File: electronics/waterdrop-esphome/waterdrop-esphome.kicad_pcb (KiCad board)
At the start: 4 copper layers, 45.7 x 80 mm, 16 parts, among them J1 Barrel_Jack, U1 LM2596DS-ADJ, U2 ESP32-S3-Tiny

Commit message: Schematics are ready for PCB layout
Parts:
- added D3: 1N4148, Diode_SMD:D_SOD-123, F.Cu at (174.0, 105.9)
- added H1: 12V_OUT_RELIEF, MountingHole:MountingHole_4.3mm_M4, F.Cu at (189.1, 71.0)
- added H2: Comm_RO_RELIEF, MountingHole:MountingHole_4.3mm_M4, F.Cu at (189.1, 81.2)
- added J2: 12V_OUT, Connector_Wire:SolderWire-1.5sqmm_1x02_P6mm_D1.7mm_OD3mm_Relief, F.Cu at (175.2, 68.6)
- added J3: Comm_RO, Connector_Wire:SolderWire-0.25sqmm_1x04_P4.2mm_D0.65mm_OD1.7mm_Relief, F.Cu at (187.9, 91.3)
- added J4: Comm_Faucet, Connector_PinHeader_2.54mm:PinHeader_1x05_P2.54mm_Horizontal, F.Cu at (174.7, 91.6)
- added J5: Valve, Connector_PinHeader_2.54mm:PinHeader_1x02_P2.54mm_Horizontal, F.Cu at (156.7, 104.2)
- added K1: G5LE-1, Relay_THT:Relay_SPDT_Omron-G5LE-1, F.Cu at (163.4, 69.4)
- added Q1: BC817, Package_TO_SOT_SMD:SOT-23, F.Cu at (196.6, 85.3)
- added R10: 50k, Resistor_SMD:R_0805_2012Metric_Pad1.20x1.40mm_HandSolder, F.Cu at (161.5, 100.5)
- added R11: 10k, Resistor_SMD:R_0805_2012Metric_Pad1.20x1.40mm_HandSolder, F.Cu at (166.3, 91.6)
- added R12: 50k, Resistor_SMD:R_0805_2012Metric_Pad1.20x1.40mm_HandSolder, F.Cu at (166.3, 94.6)
- added R13: 100k, Resistor_SMD:R_0805_2012Metric_Pad1.20x1.40mm_HandSolder, F.Cu at (166.3, 97.5)
- added R14: 1Ω, Resistor_SMD:R_0805_2012Metric_Pad1.20x1.40mm_HandSolder, F.Cu at (166.3, 100.5)
- added R4: 100k, Resistor_SMD:R_0805_2012Metric_Pad1.20x1.40mm_HandSolder, F.Cu at (156.8, 94.6)
- added R5: 100k, Resistor_SMD:R_0805_2012Metric_Pad1.20x1.40mm_HandSolder, F.Cu at (156.8, 97.5)
- added R6: 100k, Resistor_SMD:R_0805_2012Metric_Pad1.20x1.40mm_HandSolder, F.Cu at (156.8, 100.5)
- added R7: 50k, Resistor_SMD:R_0805_2012Metric_Pad1.20x1.40mm_HandSolder, F.Cu at (161.5, 91.6)
- added R8: 10k, Resistor_SMD:R_0805_2012Metric_Pad1.20x1.40mm_HandSolder, F.Cu at (161.5, 94.6)
- added R9: 100k, Resistor_SMD:R_0805_2012Metric_Pad1.20x1.40mm_HandSolder, F.Cu at (161.5, 97.5)
- added U3: 74AHCT125, Package_SO:SOIC-14_3.9x8.7mm_P1.27mm, F.Cu at (198.4, 71.2)
- added U4: TB67H450A, Package_SO:SOIC-8-1EP_3.9x4.9mm_P1.27mm_EP2.29x3mm_ThermalVias, F.Cu at (198.4, 79.7)
- D1: footprint Diode_SMD:D_SMA -> Diode_SMD:D_SMA_Handsoldering
- J1: value Barrel_Jack -> 12V_IN
- JP1: value 3V3 -> 5V
- R1: value 2k -> 3.6k
- R3: value 100k -> 10k
- moved R3 27.3 mm to (156.8, 91.6)
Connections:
- net /Power supply/SUPPLY_12V renamed /12V_IN
- J1 pad 3: (no net) -> unconnected-(J1-Pad3)
- JP1 pad 2: +3.3V -> +5V
- R3 pad 1: GND -> Net-(Q1-B)
- R3 pad 2: Net-(U2-5V) -> /12V_control
- U2 pad 1: Net-(U2-5V) -> +5V
- U2 pad 17: unconnected-(U2-IO13-Pad17) -> /VALVE_IN2
- U2 pad 18: unconnected-(U2-IO12-Pad18) -> /VALVE_IN1
- U2 pad 4: unconnected-(U2-IO1-Pad4) -> /12V_control
- U2 pad 5: unconnected-(U2-IO2-Pad5) -> /Serial_control
- U2 pad 6: unconnected-(U2-IO3-Pad6) -> /RO_TX
- U2 pad 7: unconnected-(U2-IO4-Pad7) -> /RO_RX
- U2 pad 8: unconnected-(U2-IO5-Pad8) -> /FC_TX
- U2 pad 9: unconnected-(U2-IO6-Pad9) -> /FC_RX
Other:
- board size 45.7 x 80 mm -> 105 x 80 mm

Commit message: PCB: lay out components
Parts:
- added H3: MountingHole, MountingHole:MountingHole_4.3mm_M4, F.Cu at (142.2, 86.3)
- added H4: MountingHole, MountingHole:MountingHole_4.3mm_M4, F.Cu at (148.6, 126.3)
- C3, C4, D1, D2, D3, L2, Q1, R1, R10, R11, R12, R13, R14, R2, R3, R4, R5, R6, R7, R8, R9, U1, U3, U4: moved to B.Cu
- H1, H2: footprint MountingHole:MountingHole_4.3mm_M4 -> MountingHole_extra:MountingHole_4.3mm
- moved Q1 75.6 mm to (124.5, 107.9), turned to 180 degrees
- moved H1 75.4 mm to (141.5, 129.5)
- moved K1 60.1 mm to (127.5, 117.7), turned to 180 degrees
- moved H2 58.9 mm to (155.5, 129.5)
- moved U3 53.5 mm to (153.0, 99.7)
- moved U2 47.5 mm to (160.4, 94.6), turned to -90 degrees
- moved D3 46.8 mm to (127.6, 112.4), turned to 180 degrees
- moved J2 44.5 mm to (138.5, 93.7)
- moved J3 42.6 mm to (149.2, 109.1)
- moved U4 42.2 mm to (167.6, 108.5), turned to -90 degrees
- moved C2 35.7 mm to (118.7, 87.0), turned to 90 degrees
- moved F1 35.7 mm to (113.7, 130.6), turned to 90 degrees
- moved J1 34.8 mm to (127.5, 123.5), turned to 90 degrees
- moved R9 34.7 mm to (168.9, 131.4), turned to -90 degrees
- moved L1 32.7 mm to (129.6, 90.1), turned to 180 degrees
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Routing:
- net GND: track 1.27 -> 0.00 mm, vias 1 -> 0
- net +3.3V: track 0.79 -> 0.00 mm, vias 1 -> 0
- removed copper zone on In2.Cu, net GND
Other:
- board size 105 x 80 mm -> 64.8 x 53.3 mm

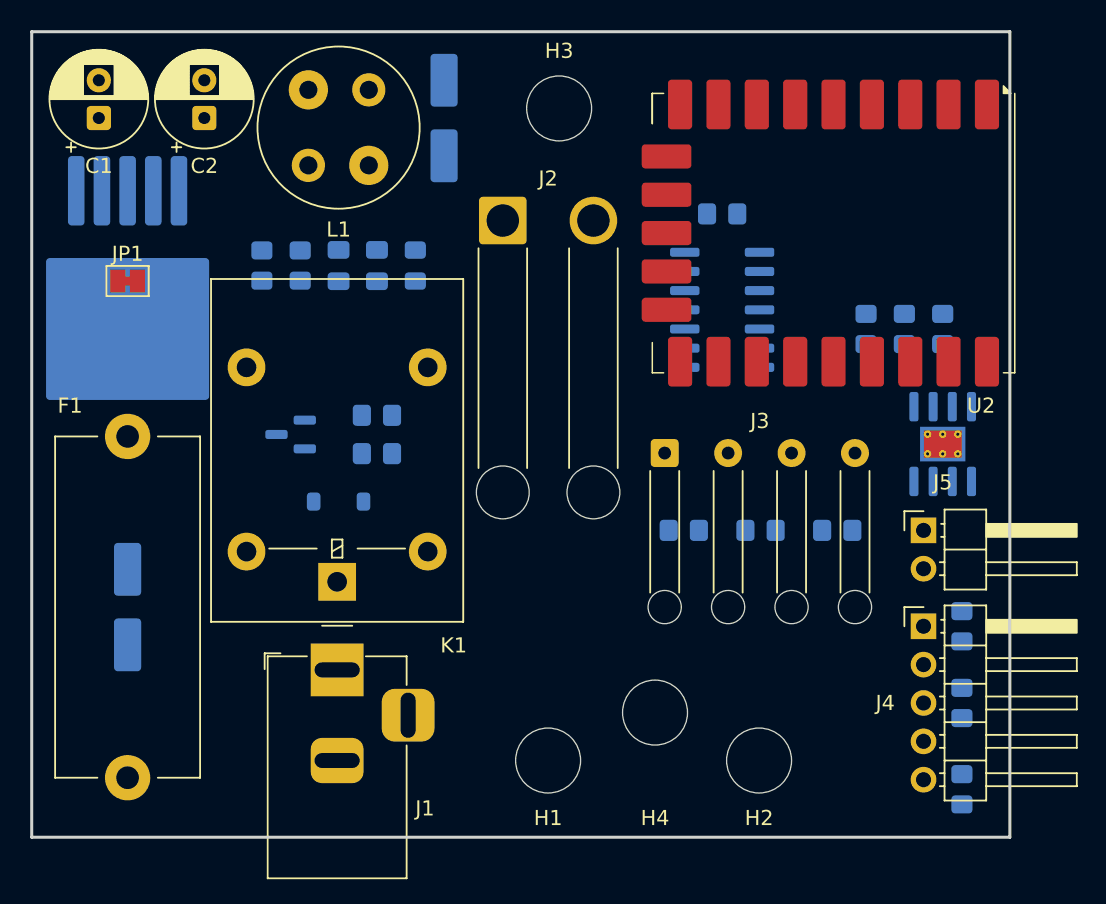
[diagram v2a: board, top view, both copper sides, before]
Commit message: PCB: trace and fix all DRC
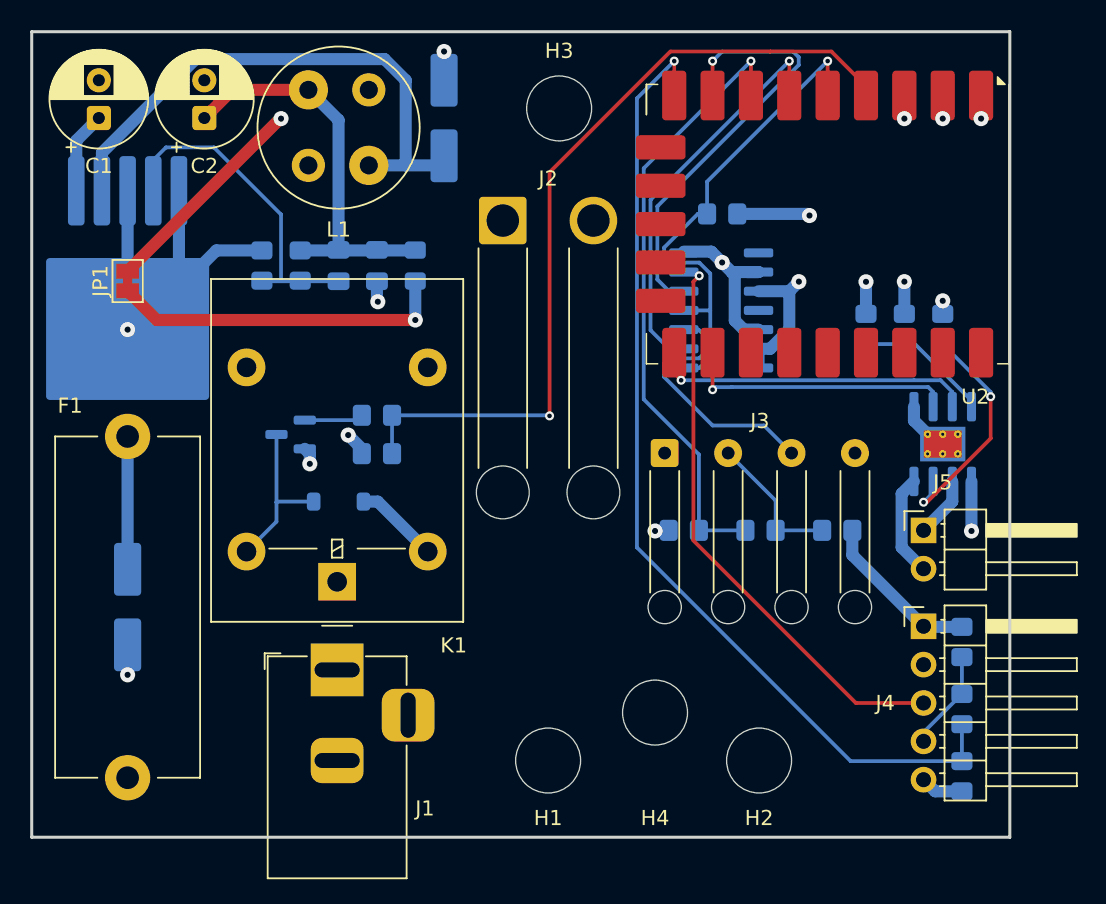
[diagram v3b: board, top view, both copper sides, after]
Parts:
- moved R11 1.04 mm to (168.9, 121.7)
- moved R9 0.87 mm to (168.9, 130.5)
- moved U2 0.71 mm to (160.0, 94.0)
- moved R10 0.41 mm to (168.9, 126.1)
- moved U3 0.08 mm to (153.0, 99.7)
- turned JP1 to 90 degrees
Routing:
- net +5V: track 0.00 -> 131.1 mm, vias 0 -> 4
- net +12V: track 0.00 -> 127.4 mm, vias 0 -> 1
- net /FC_RX: track 0.00 -> 66.2 mm, vias 0 -> 1
- net GND: track 0.00 -> 58.2 mm, vias 0 -> 10
- net /12V_control: track 0.00 -> 55.9 mm, vias 0 -> 1
- net +3.3V: track 0.00 -> 52.7 mm, vias 0 -> 3
- net /RO_RX: track 0.00 -> 41.8 mm, vias 0 -> 1
- net /FC_TX_HV: track 0.00 -> 38.5 mm, vias 0 -> 1
- net Net-(D2-K): track 0.00 -> 36.7 mm
- net /Serial_control: track 0.00 -> 33.9 mm, vias 0 -> 1
- net /FC_TX: track 0.00 -> 30.0 mm, vias 0 -> 1
- net /RO_TX: track 0.00 -> 27.5 mm, vias 0 -> 1
- net Net-(C2-Pad1): track 0.00 -> 26.7 mm
- net /12V_IN: track 0.00 -> 22.7 mm
- net Net-(JP1-A): track 0.00 -> 22.4 mm, vias 0 -> 1
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- added copper zone on In1.Cu, net GND
